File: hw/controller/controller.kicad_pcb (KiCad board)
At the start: 2 copper layers, 77.5 x 76.2 mm, 110 parts, among them J1 ARM-SWD, J2 USB_OTG, J3 UART, P1 TH0, P14 I2C0, P15 I2C1, P16 I2C2, P17 I2C3, P2 FRIDGE, P3 FAN, P4 PUMP, P5 MIST, P6 TH1, P7 TH2, P8 TH3, SW1 RST, SW2 BOOT, U1 stm32f072x, U2 MIC550X, U3 tca9546a, U4 SHT3x-DIS, U5 SHT3x-DIS, U6 SHT3x-DIS, U7 SHT3x-DIS, U8 SHT3x-DIS, Y2 32768Hz

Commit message: Placement mostly done
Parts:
- removed R27: DNP, Resistors_SMD:R_0603
- removed the REF** at (148.6, 21.6)
- C6: value 100nF -> 4.7uF
- R26: value DNP -> 10k
- moved R9 135.7 mm to (153.2, 82.8)
- moved R10 131.7 mm to (152.9, 85.6)
- moved R2 121.3 mm to (165.1, 80.0), turned to 270 degrees
- moved C9 118.3 mm to (151.4, 93.5), turned to 270 degrees
- moved C7 115.3 mm to (154.4, 103.6)
- moved C2 113.9 mm to (152.9, 93.5), turned to 270 degrees
- moved R8 113.8 mm to (169.4, 101.2), turned to 180 degrees
- moved D3 113.0 mm to (168.7, 110.7), turned to 180 degrees
- moved D2 110.4 mm to (168.7, 112.3), turned to 180 degrees
- moved C5 110.3 mm to (154.4, 105.2)
- moved C6 107.2 mm to (151.1, 114.8), turned to 90 degrees
- moved R4 105.1 mm to (165.6, 112.3), turned to 180 degrees
- moved R1 104.9 mm to (151.9, 117.3)
- moved D1 103.8 mm to (168.7, 113.8), turned to 180 degrees
- moved R5 103.6 mm to (165.6, 110.7), turned to 180 degrees
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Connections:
- net /USB_DM renamed /USB_N
- net /USB_DP renamed /USB_P
- net Net-(J2-Pad2) renamed /D_N
- net Net-(J2-Pad3) renamed /D_P
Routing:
- net /USB_P: track 0.00 -> 17.1 mm
- net /USB_N: track 0.00 -> 16.4 mm
- net /D_N: track 0.00 -> 4.16 mm
- net /D_P: track 0.00 -> 3.98 mm
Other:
- board text removed: "swd"

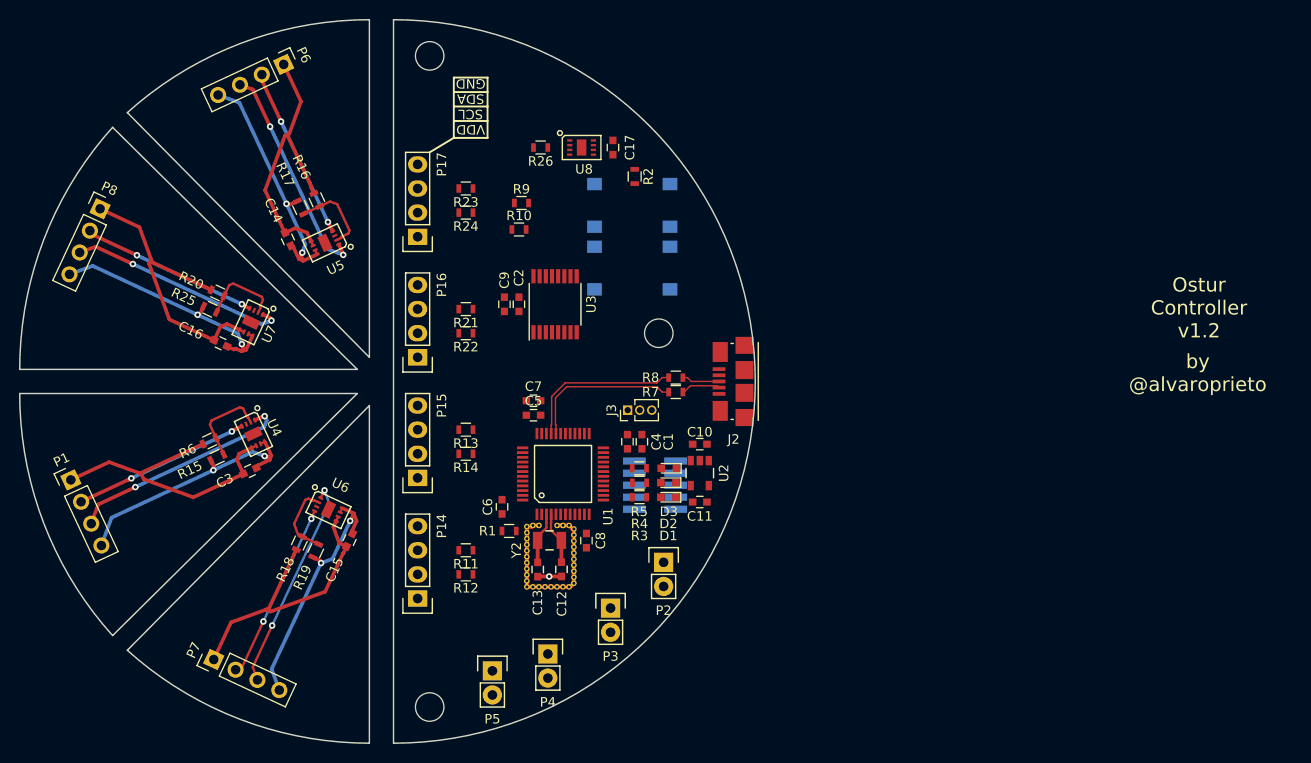
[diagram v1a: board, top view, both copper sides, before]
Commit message: Layout done for Ostur Controller v1.3
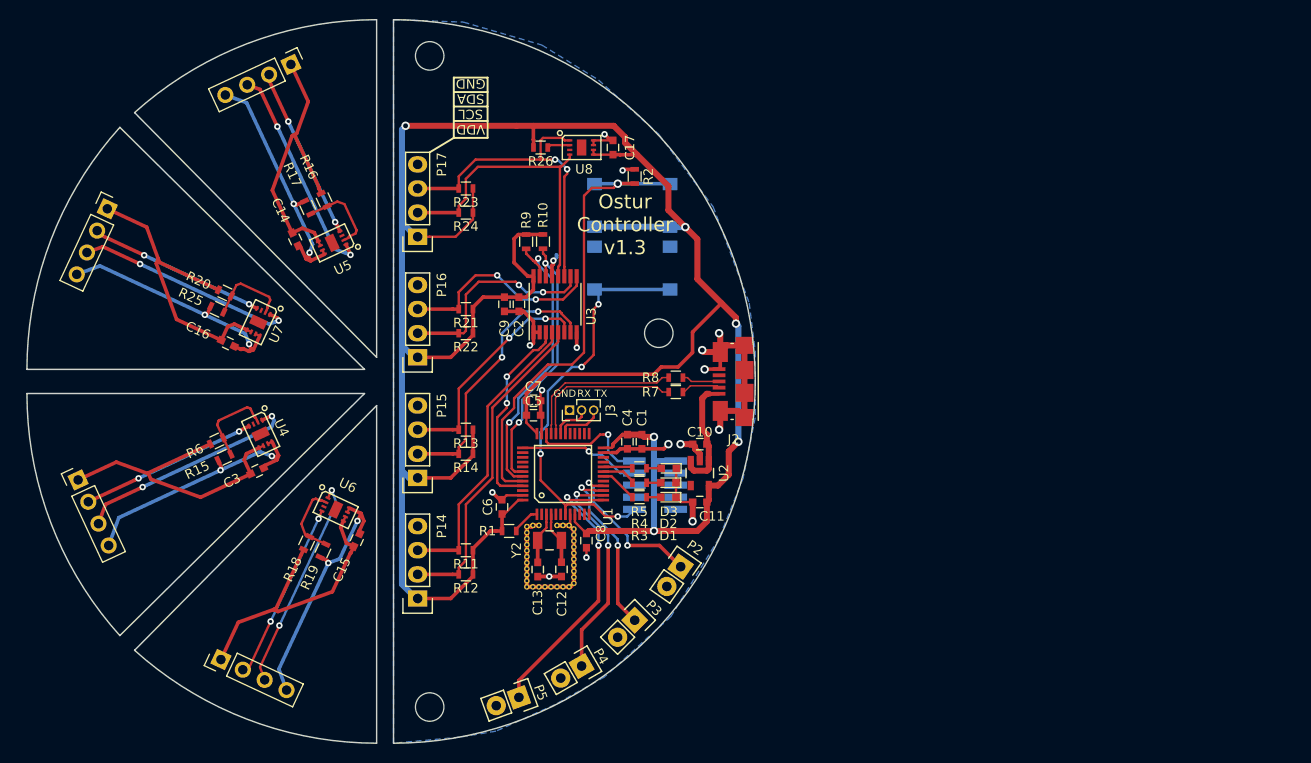
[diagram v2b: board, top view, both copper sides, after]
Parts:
- moved J3 6.12 mm to (158.2, 104.6)
- moved R9 4.11 mm to (153.7, 86.9), turned to 270 degrees
- moved P5 3.95 mm to (152.9, 134.9), turned to 290 degrees
- moved P4 3.78 mm to (159.5, 131.6), turned to 300 degrees
- moved P3 2.84 mm to (165.1, 126.7), turned to 315 degrees
- moved R10 2.83 mm to (155.4, 86.9), turned to 270 degrees
- moved P2 1.85 mm to (169.9, 121.1), turned to 325 degrees
- moved C14 0.76 mm to (129.3, 86.6)
- moved C15 0.76 mm to (135.8, 118.3)
- moved C16 0.76 mm to (122.2, 97.6)
- moved C3 0.76 mm to (125.3, 111.0)
- moved P1 0.76 mm to (106.5, 112.0)
- moved P6 0.76 mm to (128.9, 68.2)
- moved P7 0.76 mm to (121.5, 130.9)
- moved P8 0.76 mm to (109.6, 83.4)
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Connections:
- U8 pad 1: /SDA0 -> /SDA3
- U8 pad 4: /SCL0 -> /SCL3
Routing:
- net VDD: track 0.00 -> 274.0 mm, vias 0 -> 6
- net GND: track 22.9 -> 90.4 mm, vias 1 -> 16
- net /boot0: track 0.00 -> 50.9 mm, vias 0 -> 1
- net /nRST: track 0.00 -> 44.2 mm, vias 0 -> 4
- net /SDA3: track 0.00 -> 34.9 mm, vias 0 -> 2
- net /SCL0: track 0.00 -> 34.2 mm
- net /SCL3: track 0.00 -> 32.0 mm
- net /SDA0: track 0.00 -> 31.4 mm
- net /SDA: track 0.00 -> 31.0 mm, vias 0 -> 2
- net /MIST: track 0.00 -> 29.9 mm, vias 0 -> 2
- net /SCL: track 0.00 -> 28.9 mm, vias 0 -> 2
- net /SCL1: track 0.00 -> 28.6 mm, vias 0 -> 2
- net /SDA1: track 0.00 -> 24.0 mm, vias 0 -> 2
- net /PUMP: track 0.00 -> 23.5 mm, vias 0 -> 2
- net /SCL2: track 0.00 -> 22.3 mm, vias 0 -> 2
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- added copper zone on B.Cu, net GND
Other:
- board size 77.5 x 76.2 mm -> 76.7 x 76.2 mm
- board text added: "GND"
- board text added: "Ostur Controller v1.3"
- board text added: "RX"
- board text added: "TX"
- board text removed: "Ostur Controller v1.2"

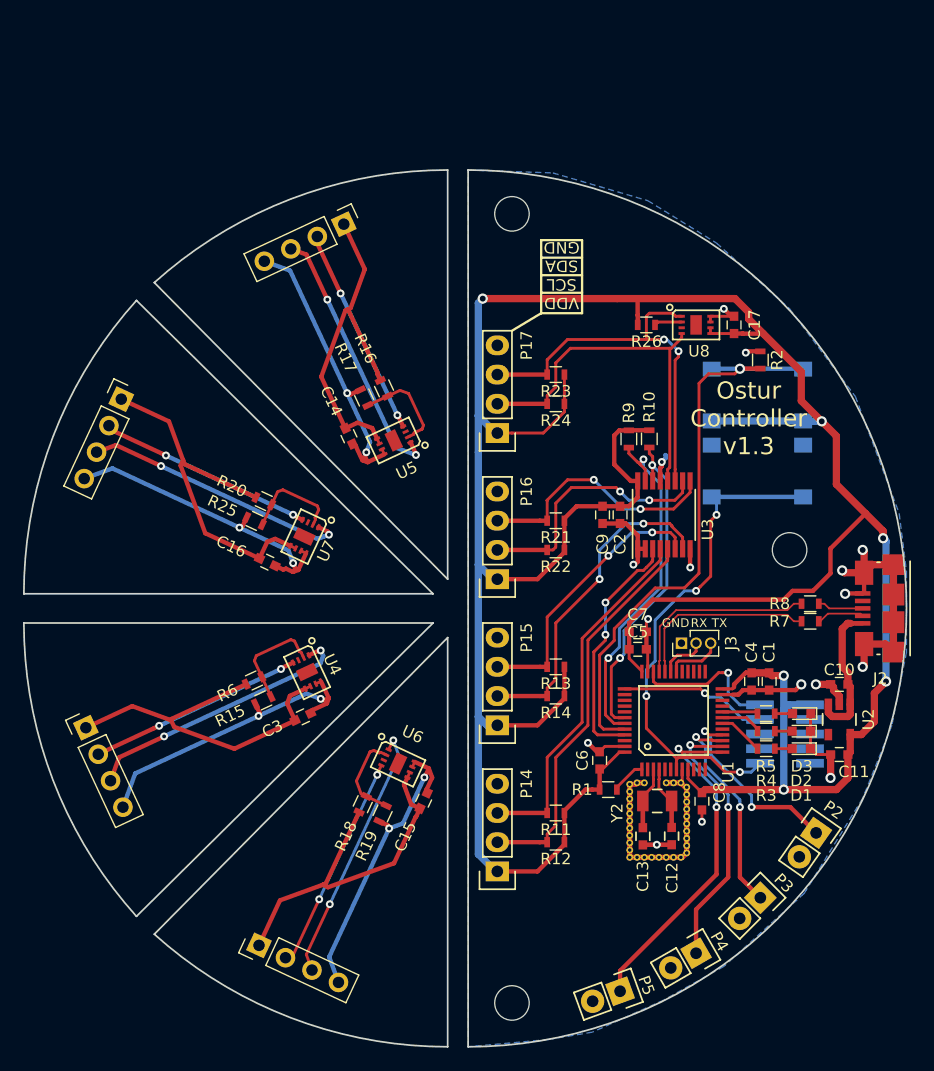
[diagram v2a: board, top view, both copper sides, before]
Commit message: Removed sensor breakouts from controller
Updated silkscreen
Removed SWD connector
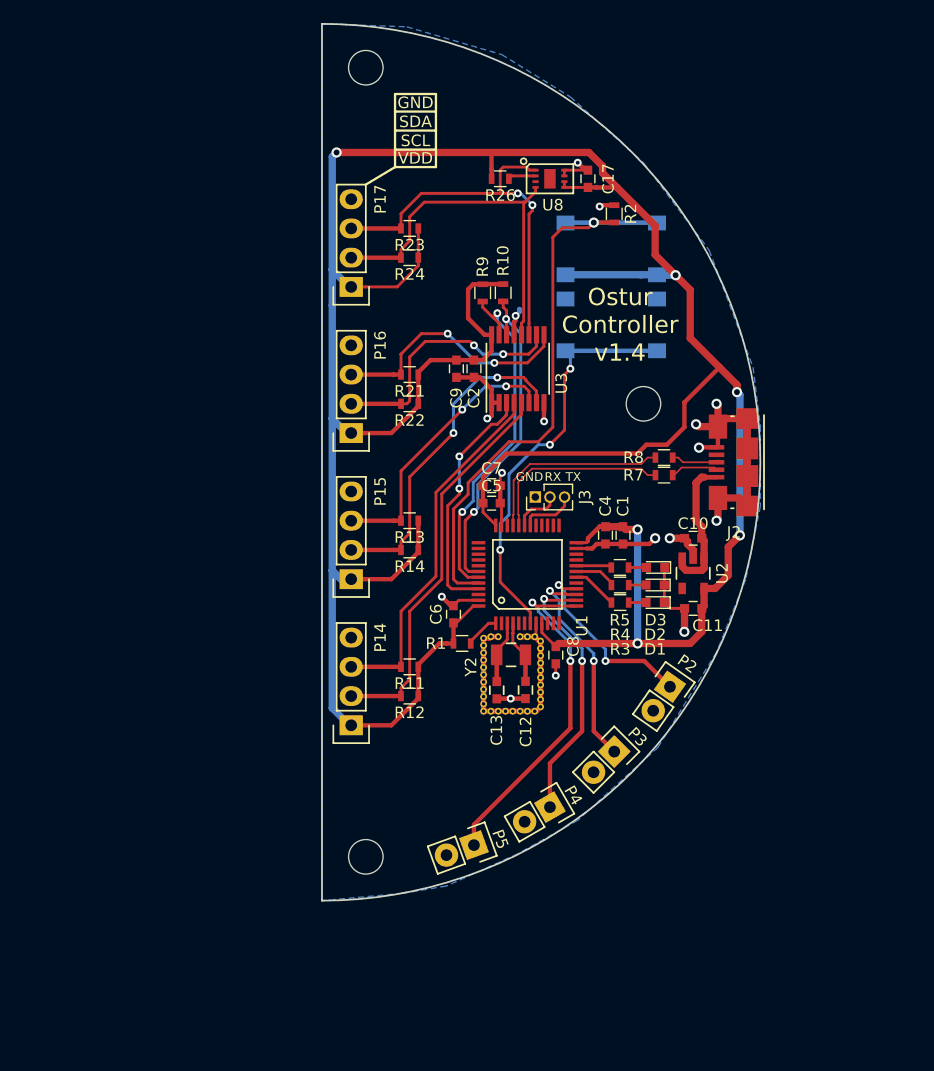
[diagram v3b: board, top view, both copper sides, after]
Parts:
- removed C14, C15, C16, C3: 100nF, Capacitors_SMD:C_0603
- removed J1: ARM-SWD, footprints:ARM_SWD_SMD
- removed P1: TH0, Pin_Headers:Pin_Header_Straight_1x04_Pitch2.54mm
- removed P6: TH1, Pin_Headers:Pin_Header_Straight_1x04_Pitch2.54mm
- removed P7: TH2, Pin_Headers:Pin_Header_Straight_1x04_Pitch2.54mm
- removed P8: TH3, Pin_Headers:Pin_Header_Straight_1x04_Pitch2.54mm
- removed R15, R17, R19, R25: 10k, Resistors_SMD:R_0603
- removed R16, R18, R20, R6: DNP, Resistors_SMD:R_0603
- removed U4, U5, U6, U7: SHT3x-DIS, footprints:SHT3x
- moved C8 18.0 mm to (147.3, 105.7)
- moved D1 18.0 mm to (156.0, 101.1)
- moved D2 18.0 mm to (156.0, 99.6)
- moved P15 18.0 mm to (129.5, 99.1)
- moved P16 18.0 mm to (129.5, 86.4)
- moved P17 18.0 mm to (129.5, 73.7)
- moved R3 18.0 mm to (152.9, 101.1)
- moved R4 18.0 mm to (152.9, 99.6)
- moved R5 18.0 mm to (152.9, 98.0)
- moved R7 18.0 mm to (156.7, 90.0)
- moved R8 18.0 mm to (156.7, 88.5)
- moved REF** 18.0 mm to (142.3, 104.1)
- moved REF** 18.0 mm to (142.3, 110.5)
- moved REF** 18.0 mm to (144.2, 110.5)
- moved REF** 18.0 mm to (146.0, 110.2)
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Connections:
- U1 pad 34: /SWDIO -> Net-(U1-Pad34)
- U1 pad 37: /SWCLK -> Net-(U1-Pad37)
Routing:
- net /VDD_TH0: track 31.7 -> 0.00 mm
- net /VDD_TH3: track 31.6 -> 0.00 mm
- net /VDD_TH2: track 31.2 -> 0.00 mm
- net /VDD_TH1: track 30.4 -> 0.00 mm
- net /GND_TH0: track 27.1 -> 0.00 mm, vias 2 -> 0
- net /GND_TH3: track 26.9 -> 0.00 mm, vias 2 -> 0
- net /GND_TH2: track 26.5 -> 0.00 mm, vias 2 -> 0
- net /GND_TH1: track 26.3 -> 0.00 mm, vias 2 -> 0
- net /SDA_TH0: track 23.8 -> 0.00 mm, vias 2 -> 0
- net /SDA_TH3: track 23.4 -> 0.00 mm, vias 2 -> 0
- net /SDA_TH1: track 23.0 -> 0.00 mm, vias 2 -> 0
- net /SDA_TH2: track 22.8 -> 0.00 mm, vias 2 -> 0
- net /SCL_TH2: track 18.9 -> 0.00 mm, vias 2 -> 0
- net /SCL_TH3: track 18.8 -> 0.00 mm, vias 2 -> 0
- net /SCL_TH0: track 18.7 -> 0.00 mm, vias 2 -> 0
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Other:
- board size 76.7 x 76.2 mm -> 38.1 x 76.2 mm
- rule pad_to_mask_clearance: 0.2 -> 0.1016
- board text added: "Ostur Controller v1.4"
- board text added: "SCL"
- board text added: "SDA"
- board text added: "VDD"
- board text removed: "Ostur Controller v1.3"
- board text removed: "VDD SCL SDA GND"

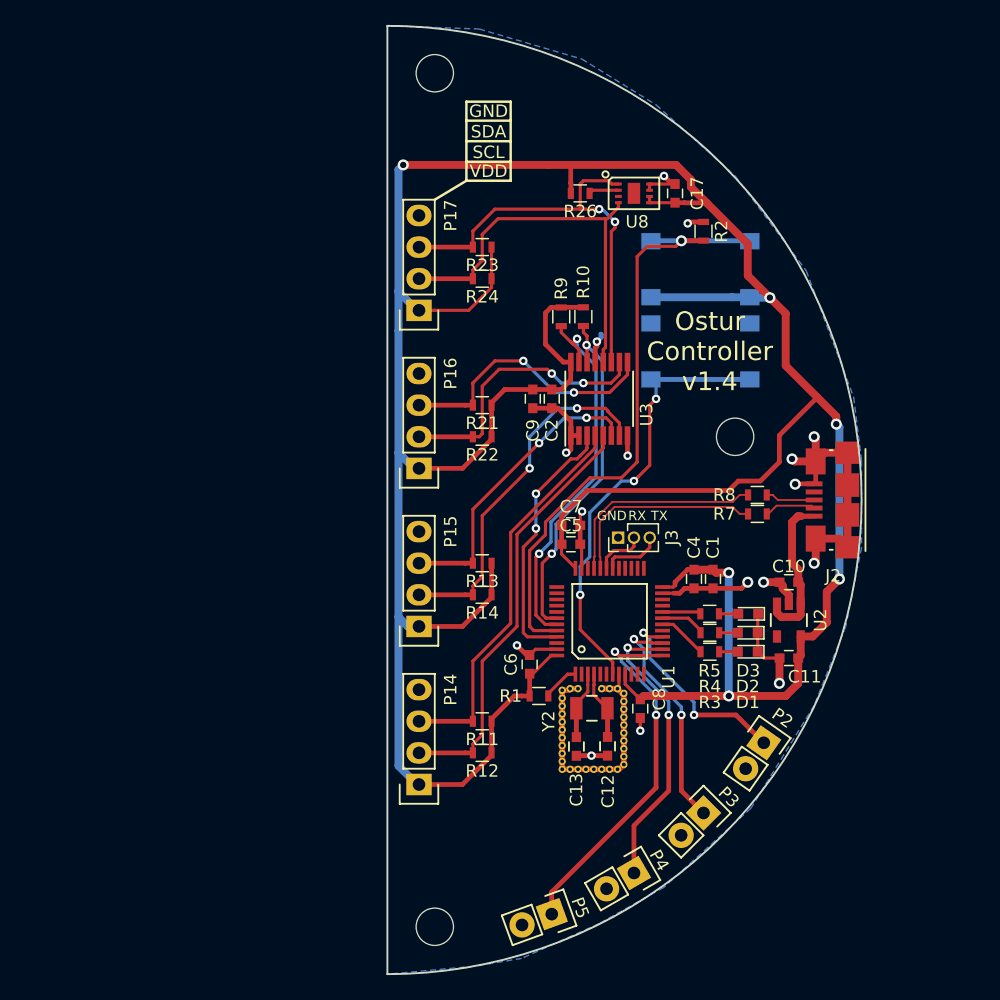
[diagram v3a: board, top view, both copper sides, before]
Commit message: Fixed silkscreens on controller/sensor
And submitted to pcbcart!
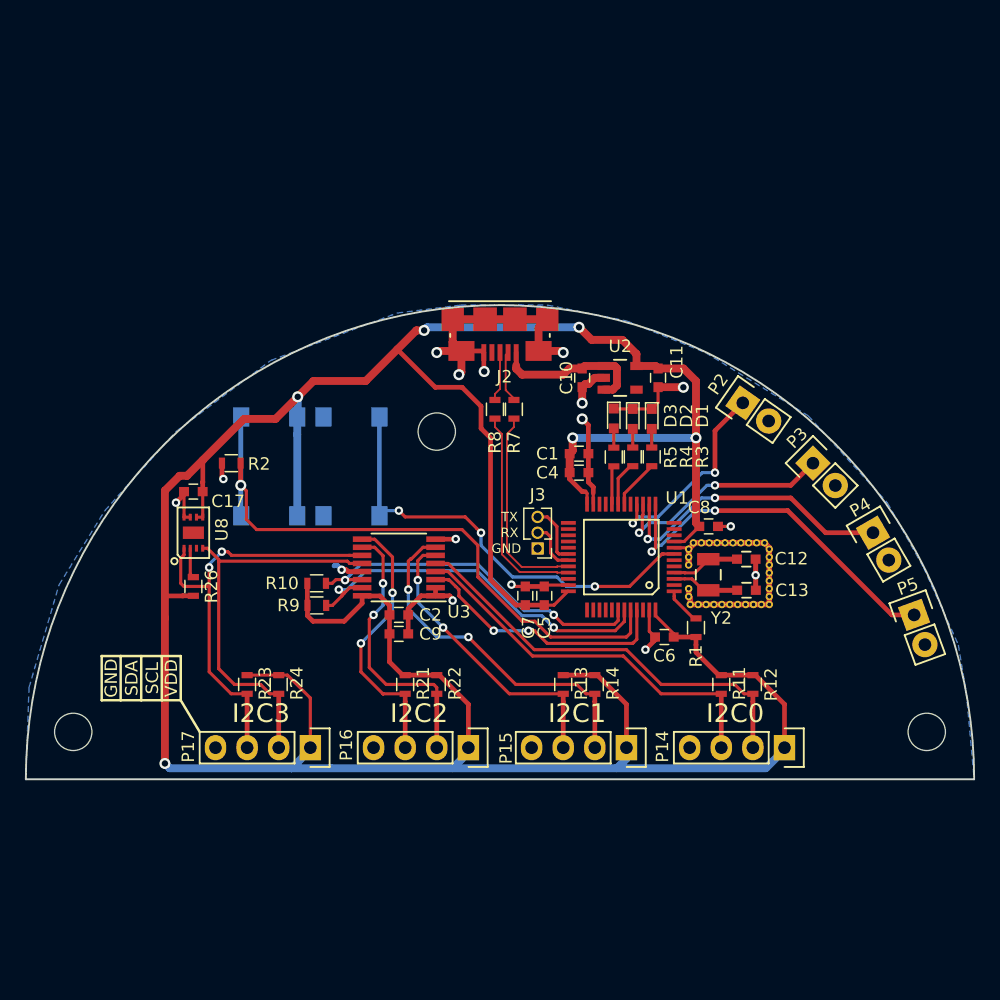
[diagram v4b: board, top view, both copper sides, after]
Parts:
- moved REF** 60.4 mm to (101.8, 107.5), turned to 90 degrees
- moved C17 45.5 mm to (111.4, 88.2), turned to 180 degrees
- moved U8 44.7 mm to (111.4, 91.5), turned to 90 degrees
- moved R26 44.3 mm to (111.4, 95.8), turned to 270 degrees
- moved REF** 42.5 mm to (170.3, 107.5), turned to 90 degrees
- moved R2 42.3 mm to (114.5, 85.9), turned to 0 degrees
- moved R23 39.9 mm to (115.7, 103.7), turned to 270 degrees
- moved SW2 38.1 mm to (117.5, 86.2), turned to 90 degrees
- moved P5 37.8 mm to (169.3, 98.1), turned to 20 degrees
- moved R24 36.5 mm to (118.3, 103.7), turned to 270 degrees
- moved P17 36.2 mm to (120.8, 108.8), turned to 270 degrees
- moved P4 33.4 mm to (166.0, 91.5), turned to 30 degrees
- moved R9 30.4 mm to (121.3, 97.4), turned to 0 degrees
- moved R10 30.3 mm to (121.3, 95.6), turned to 0 degrees
- moved SW1 29.5 mm to (124.1, 86.2), turned to 270 degrees
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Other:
- board size 38.1 x 76.2 mm -> 76.2 x 38.1 mm
- board text added: "Controller v1.4"
- board text added: "Ostur"
- board text removed: "Ostur Controller v1.4"
